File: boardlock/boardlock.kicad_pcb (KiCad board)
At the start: 2 copper layers, 101 x 76.2 mm, 175 parts, among them J1 Conn_01x02, J2 Conn_01x02, J3 Conn_01x02, J4 Conn_01x02, J5 5033981892, J6 USB_C_Receptacle_USB2.0, Q1 BSS84PWH6327XTSA1, Q2 MMBT4401, Q3 BSS84PWH6327XTSA1, Q4 MMBT4401, Q5 MMBT4401, Q6 MMBT4401, Q7 MMBT4401, SW1 SW_Push, SW2 SW_Push, SW3 SW_Push, SW4 SW_Push, SW5 SW_Push, U1 ESP32-S3-WROOM-1, U2 LSM6DSO32, U3 SAM-M8Q, U4 BQ24075RGT, U5 BQ27441DRZR-G1A, U6 TPS630701RNMR, U7 MCP1661, U8 MAX98357AETE+T, U9 TPD2E2U06

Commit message: PCB: completed fuel gauge
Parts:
- C9: moved to B.Cu
- D3: moved to F.Cu
- J3: footprint Connector_JST:JST_XA_B02B-XASK-1-A_1x02_P2.50mm_Vertical -> Connector_JST:JST_XA_B02B-XASK-1_1x02_P2.50mm_Vertical
- moved J3 281.0 mm to (173.7, 135.3)
- moved U8 269.3 mm to (178.8, 125.7)
- moved R35 221.7 mm to (225.5, 148.2)
- moved R36 221.7 mm to (225.5, 151.1)
- moved R37 221.7 mm to (225.5, 154.1)
- moved C23 221.7 mm to (240.8, 143.0)
- moved C24 221.7 mm to (240.8, 140.0)
- moved C26 221.7 mm to (240.8, 146.1)
- moved C27 221.7 mm to (240.8, 149.1)
- moved C28 221.7 mm to (240.8, 152.1)
- moved C25 221.7 mm to (233.0, 138.4)
- moved FB1 221.7 mm to (233.2, 154.5)
- moved FB2 221.7 mm to (233.2, 158.8)
- moved R25 87.4 mm to (190.8, 72.2)
- moved R24 84.9 mm to (193.4, 59.6)
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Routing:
- net BATTERY_IN: track 0.00 -> 29.6 mm
- net +BATT: track 4.03 -> 29.8 mm
- net /ui/V_USB: track 25.1 -> 11.8 mm
- net GND: track 10.9 -> 18.7 mm, vias 1 -> 6
- net BATT_CHARGE_VOUT: track 8.56 -> 3.91 mm
- net Net-(U5-V_{DD}): track 0.00 -> 2.72 mm, vias 0 -> 1
- net M_FUEL_GPOUT: track 1.51 -> 0.00 mm
- added copper zone on B.Cu, net GND
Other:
- board text removed: "USB-C Connector"

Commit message: buck-boost WIP
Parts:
- R15, R19: moved to B.Cu
- R20, R22: footprint Resistor_SMD:R_0805_2012Metric_Pad1.20x1.40mm_HandSolder -> Resistor_SMD:R_0603_1608Metric_Pad0.98x0.95mm_HandSolder; moved to B.Cu
- R21, R23: footprint Resistor_SMD:R_0805_2012Metric_Pad1.20x1.40mm_HandSolder -> Resistor_SMD:R_0603_1608Metric_Pad0.98x0.95mm_HandSolder
- moved R28 272.0 mm to (175.3, 96.3)
- moved U6 271.3 mm to (187.3, 92.8)
- moved R27 271.2 mm to (175.3, 94.2)
- moved C16 270.5 mm to (188.7, 88.1)
- moved C18 269.2 mm to (183.6, 93.9), turned to -90 degrees
- moved R26 268.8 mm to (171.4, 95.2)
- moved C17 266.6 mm to (188.7, 97.2)
- moved C15 264.6 mm to (188.9, 86.3)
- moved C14 263.7 mm to (188.9, 84.3)
- moved L1 259.4 mm to (194.9, 92.8), turned to -90 degrees
- moved C13 257.3 mm to (188.9, 103.1)
- moved C12 256.4 mm to (188.9, 101.0)
- moved C11 255.5 mm to (188.9, 99.0)
- moved R32 254.7 mm to (222.7, 86.3)
- moved R56 254.7 mm to (222.7, 89.3)
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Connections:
- net Net-(U4-ILIM) renamed /battery/ILIM
- net Net-(U4-ISET) renamed /battery/ISET
- net Net-(U4-TMR) renamed /battery/TIMER
- net Net-(U4-~{CE}) renamed /battery/N_Charge_EN
- net Net-(U6-FB) renamed /power/Buck_Boost_FB
- net Net-(U6-PG) renamed /power/Buck_Boost_PG
- net Net-(U6-PS_SYNC) renamed /power/PS_SYNC
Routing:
- net VBUS: track 1.56 -> 23.1 mm, vias 0 -> 2
- net GND: track 18.7 -> 26.9 mm, vias 6 -> 7
- net BATT_CHARGE_VOUT: track 3.91 -> 10.4 mm, vias 0 -> 1
- net Net-(J6-CC2): track 0.00 -> 6.40 mm
- net M_BATT_CHARGE_N_CHG: track 3.98 -> 0.00 mm
- net BATT_CHARGE_EN1: track 0.00 -> 3.48 mm, vias 0 -> 1
- net M_BATT_CHARGE_N_PGOOD: track 3.08 -> 0.00 mm
- net /battery/ILIM: track 2.20 -> 5.03 mm, vias 0 -> 1
- net Net-(J6-CC1): track 0.00 -> 2.54 mm
- net /battery/TIMER: track 5.63 -> 3.28 mm, vias 0 -> 1
- net /battery/ISET: track 1.70 -> 3.63 mm
- net TS_RESISTOR: track 4.05 -> 5.85 mm, vias 0 -> 1
- net Net-(U6-L2): track 0.00 -> 1.53 mm, vias 0 -> 5
- net Net-(U6-L1): track 0.00 -> 1.53 mm, vias 0 -> 5
- net +BATT: track 29.8 -> 28.6 mm, vias 0 -> 2
- added copper zone on B.Cu, net Net-(U6-L1)
- added copper zone on F.Cu, net Net-(U6-L1)
- added copper zone on B.Cu, net Net-(U6-L2)
- added copper zone on F.Cu, net Net-(U6-L2)
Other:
- board text added: "for some of the resistors near here you could drop a via and put on the bottom"
- board text removed: "3V3 Buck-Boost"

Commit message: much buck-boost progress
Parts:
- moved R27 45.3 mm to (219.6, 103.6)
- moved R26 45.3 mm to (215.8, 104.6)
- moved R28 45.3 mm to (219.6, 105.7)
- moved C18 29.9 mm to (213.4, 96.2)
- moved C16 10.3 mm to (181.3, 95.2)
- moved C13 10.3 mm to (181.5, 110.2)
- moved L1 10.3 mm to (187.5, 99.8)
- moved C11 10.3 mm to (181.5, 106.1)
- moved C14 10.3 mm to (181.4, 91.4)
- moved C15 10.3 mm to (181.4, 93.4)
- moved C12 10.3 mm to (181.5, 108.1)
- moved C17 10.3 mm to (181.3, 104.3)
- moved U6 10.3 mm to (179.9, 99.8)
- moved R18 2.88 mm to (173.4, 71.1), turned to 0 degrees
- moved R19 0.15 mm to (174.8, 77.5), turned to -90 degrees
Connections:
- net Net-(U6-VAUX) renamed /power/VAUX
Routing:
- net BATT_CHARGE_EN2: track 2.71 -> 4.45 mm
- net BATT_CHARGE_VOUT: track 10.4 -> 11.9 mm
- net VBUS: track 23.1 -> 22.2 mm
- net TS_RESISTOR: track 5.85 -> 6.03 mm, vias 1 -> 2
- added copper zone on F.Cu, net BATT_CHARGE_VOUT
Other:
- board text added: "Need to stitch GND together"

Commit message: savinig before moving USB-C
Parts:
- moved H5 13.6 mm to (150.3, 57.4)
- moved C6 9.95 mm to (176.5, 76.5)
- moved C7 9.95 mm to (182.2, 73.7)
- moved R15 9.95 mm to (176.6, 68.1)
- moved R21 9.95 mm to (182.9, 70.8)
- moved R22 9.95 mm to (172.5, 71.8)
- moved C8 9.95 mm to (174.0, 71.8)
- moved R18 9.95 mm to (183.1, 69.0)
- moved R19 9.95 mm to (184.5, 75.3)
- moved R20 9.95 mm to (179.0, 77.4)
- moved R23 9.95 mm to (179.0, 77.4)
- moved U4 9.95 mm to (178.3, 72.6)
- moved C13 4.55 mm to (184.4, 113.6)
- moved C16 4.55 mm to (184.2, 98.6)
- moved L1 4.55 mm to (190.5, 103.3)
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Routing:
- net VBUS: track 22.2 -> 7.11 mm
- net +BATT: track 28.6 -> 18.0 mm
- net TS_RESISTOR: track 6.03 -> 16.0 mm
- net BATTERY_IN: track 29.6 -> 28.7 mm

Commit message: started on boost converter
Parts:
- U7: footprint Package_TO_SOT_SMD:SOT-23-5 -> Package_TO_SOT_SMD:SOT-23-5_HandSoldering
- moved U7 307.6 mm to (230.5, 49.8), turned to 90 degrees
- moved R33 307.1 mm to (243.2, 45.5)
- moved R34 307.1 mm to (243.2, 48.4)
- moved C19 298.7 mm to (223.6, 48.8), turned to -90 degrees
- moved C22 298.4 mm to (235.1, 57.7), turned to 90 degrees
- moved C21 297.5 mm to (232.3, 57.7), turned to 90 degrees
- moved D2 297.4 mm to (229.4, 56.0), turned to 90 degrees
- moved C20 296.2 mm to (225.8, 48.8), turned to -90 degrees
- moved L2 295.9 mm to (217.2, 50.5), turned to -90 degrees
- moved J5 264.2 mm to (198.3, 125.7), turned to -90 degrees
- moved U9 16.1 mm to (160.8, 73.0)
- moved C31 16.0 mm to (165.8, 74.4)
- moved D3 16.0 mm to (165.9, 73.3)
- moved J6 16.0 mm to (157.7, 70.6)
- moved R44 16.0 mm to (167.5, 69.8)
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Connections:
- U9 pad 2: unconnected-(U9-NC-Pad2) -> USB_D-
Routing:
- net USB_D-: track 35.6 -> 45.8 mm
- net USB_D+: track 33.0 -> 42.6 mm
- net VBUS: track 7.11 -> 14.9 mm, vias 2 -> 1
- net GND: track 26.9 -> 31.8 mm, vias 7 -> 12
- net Net-(U6-L2): track 1.53 -> 1.60 mm, vias 5 -> 6
- net Net-(U6-L1): track 1.53 -> 1.60 mm, vias 5 -> 6
- added copper zone on F.Cu, net +3V3
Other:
- board text removed: "12V Boost Converter"

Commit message: gps pcb stuff
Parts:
- Q1, Q2, R14, R5, R6, R7: moved to B.Cu
- moved TP42 276.2 mm to (142.1, 138.3)
- moved TP40 259.5 mm to (144.0, 90.8)
- moved TP41 167.5 mm to (142.0, 90.8)
- moved C5 53.3 mm to (166.5, 136.3), turned to 0 degrees
- moved R11 51.6 mm to (117.1, 114.7), turned to 0 degrees
- moved R10 50.9 mm to (117.1, 116.6), turned to 0 degrees
- moved R12 50.4 mm to (139.1, 88.9), turned to 0 degrees
- moved R13 24.4 mm to (117.1, 112.8), turned to 0 degrees
- moved R5 6.60 mm to (118.2, 115.9)
- moved R6 2.68 mm to (116.2, 110.2)
- moved R7 1.81 mm to (114.2, 110.3)
- moved U3 1.76 mm to (142.0, 114.8), turned to 180 degrees
- moved R9 1.43 mm to (114.4, 123.7)
- moved U2 1.43 mm to (113.8, 127.3)
- moved C3 1.43 mm to (115.9, 129.8)
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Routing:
- net M_GPS_EXTINT: track 15.7 -> 137.1 mm, vias 1 -> 6
- net M_IMU_INT2: track 2.27 -> 82.5 mm, vias 0 -> 6
- net Net-(U3-SCL): track 87.5 -> 16.5 mm, vias 2 -> 0
- net M_I2C_SDA: track 16.8 -> 60.7 mm
- net M_UART_TX: track 0.00 -> 42.1 mm, vias 0 -> 2
- net GPS_POWER: track 89.4 -> 130.6 mm, vias 2 -> 5
- net M_UART_RX: track 0.08 -> 40.9 mm, vias 0 -> 2
- net Net-(U3-SDA): track 42.5 -> 18.6 mm
- net M_I2C_SCL: track 84.0 -> 66.5 mm, vias 3 -> 2
- net Net-(U3-TIMEPULSE): track 0.00 -> 16.6 mm
- net Net-(U3-~{SAFEBOOT}): track 0.00 -> 16.6 mm
- net Net-(U3-~{RESET}): track 0.00 -> 16.1 mm
- net M_GPS_POWER: track 27.8 -> 26.1 mm, vias 2 -> 3
- net Net-(U2-INT1): track 2.38 -> 1.81 mm

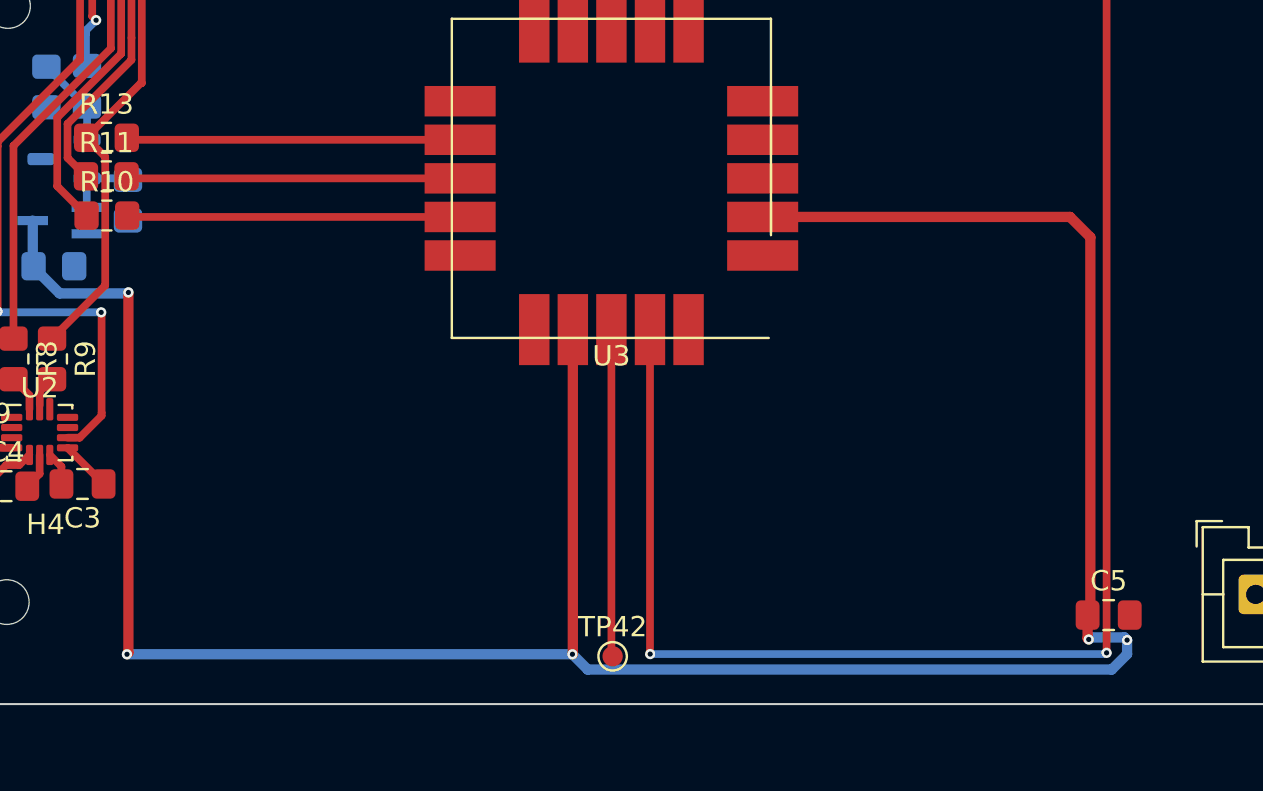
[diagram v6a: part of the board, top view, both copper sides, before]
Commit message: updating gps caps
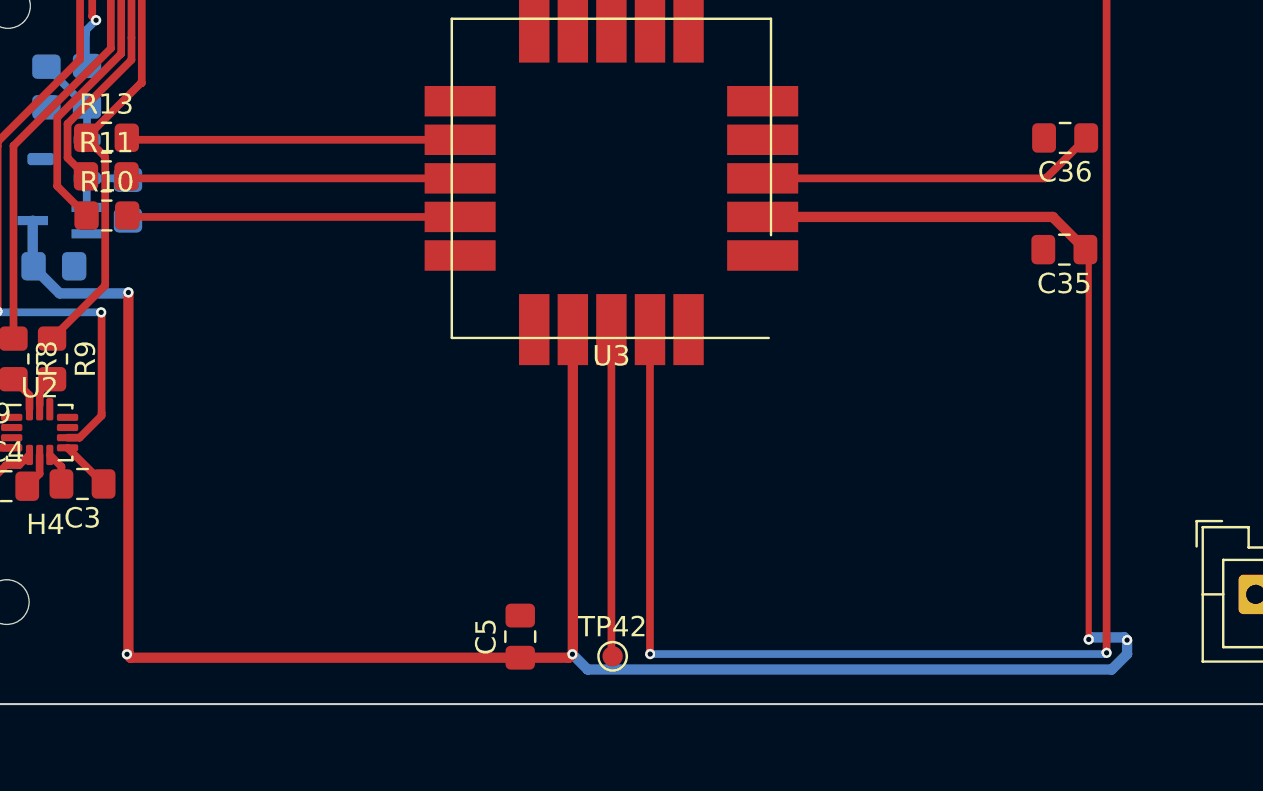
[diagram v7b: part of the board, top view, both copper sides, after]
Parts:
- added C35: 1.0uF, Capacitor_SMD:C_0805_2012Metric_Pad1.18x1.45mm_HandSolder, F.Cu at (164.3, 118.3)
- added C36: 1.0uF, Capacitor_SMD:C_0805_2012Metric_Pad1.18x1.45mm_HandSolder, F.Cu at (164.3, 112.8)
- moved C5 29.0 mm to (137.5, 137.4), turned to 90 degrees
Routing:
- net +3V3: track 12.2 -> 28.9 mm
- net GPS_POWER: track 130.6 -> 130.0 mm

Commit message: commit
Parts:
- J5: moved to B.Cu
